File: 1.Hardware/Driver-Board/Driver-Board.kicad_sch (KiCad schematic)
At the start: 75 parts, among them J1 Conn_01x04, J2 Conn_01x02, J3 Conn_01x02, J4 Conn_01x04, J5 Conn_01x02, J6 Conn_01x02, Q1 FDN352AP, SW1 SW_Push, U1 MP2456, U2 MCP1700-3302E_SOT23, U3 TJA1051T-3, U4 AS5600, U5 TB67H450FNG,EL, U6 TB67H450FNG,EL, U7 STM32F103C6Tx, Y1 12MHz

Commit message: updated board
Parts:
- removed D1: B5819W, Diode_SMD:D_SOD-123, symbol Device:D_Schottky_Small
- L1: value L_Small -> 22uH
- SW1: footprint Button_Switch_SMD:SW_SPST_TL3305B -> custom:KMR731NG LFS
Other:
- note added: "Dual H-Bridge Drivers"
- note added: "Program using I2C"
- note removed: "Dual H-Bridge Driver"
- moved on the sheet: C11, C12, C13, C14, C15, C16, C17, C18, C2, C23, C24, C25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

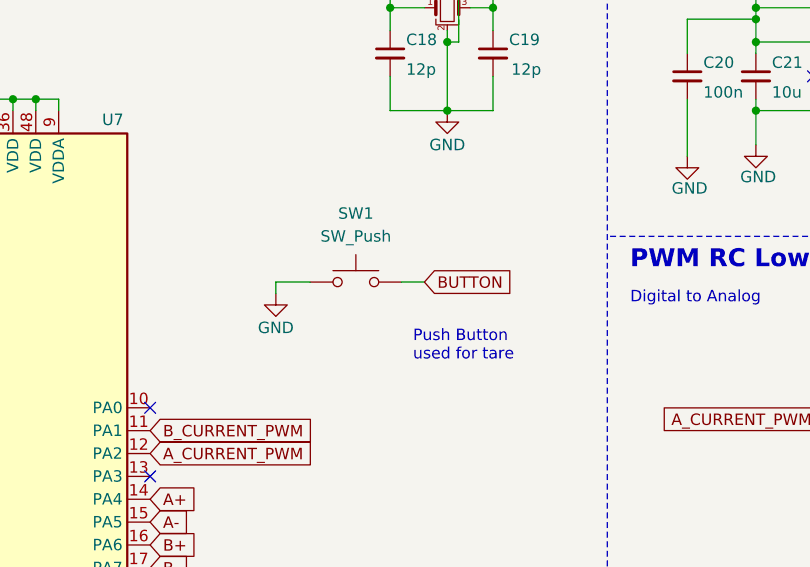
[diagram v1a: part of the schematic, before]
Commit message: libopencm3 integration and power test
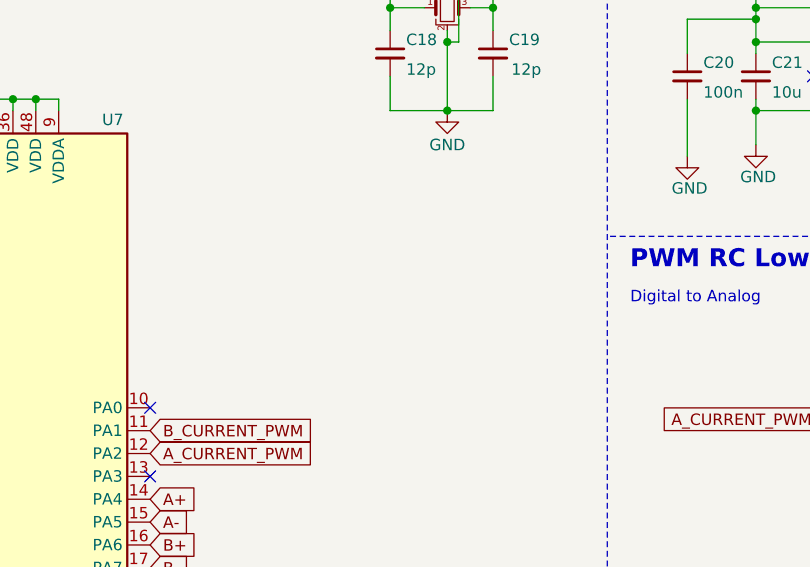
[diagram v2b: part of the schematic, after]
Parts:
- removed SW1: SW_Push, custom:KMR731NG LFS, symbol Switch:SW_Push
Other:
- note removed: "Push Button used for tare"
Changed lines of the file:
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@@
 		)
 	)
-	(wire
-		(pts
-			(xy 78.74 132.08) (xy 82.55 132.08)
-		)
-		(stroke
-			(width 0)
-			(type default)
-		)
-	)
 	(polyline
 		(pts
@@
 	(wire
 		(pts
-			(xy 78.74 133.35) (xy 78.74 132.08)
-		)
-		(stroke
-			(width 0)
-			(type default)
-		)
-	)
-	(wire
-		(pts
 			(xy 97.79 97.79) (xy 99.06 97.79)
 		)
@@
 		)
 	)
-	(wire
-		(pts
-			(xy 92.71 132.08) (xy 95.25 132.08)
-		)
-		(stroke
-			(width 0)
-			(type default)
-		)
-	)
 	(text "CAN, SWD, I2C, and Power"
 		(exclude_from_sim no)
@@
 		)
 	)
-	(text "Push Button\nused for tare"
-		(exclude_from_sim no)
-		(at 93.98 140.97 0)
-		(effects
-			(font
-				(size 1.27 1.27)
-			)
-			(justify left bottom)
-		)
-	)
 	(text "Reverse Polairty & \nOvercurrent Protection"
 		(exclude_from_sim no)
@@
 		)
 	)
-	(global_label "BUTTON"
-		(shape input)
-		(at 95.25 132.08 0)
-		(fields_autoplaced yes)
-		(effects
-			(font
-				(size 1.27 1.27)
-			)
-			(justify left)
-		)
-		(property "Intersheetrefs" "${INTERSHEET_REFS}"
-			(at 104.8598 132.1594 0)
-			(effects
-				(font
-					(size 1.27 1.27)
-				)
-				(justify left)
-				(hide yes)
-			)
-		)
-	)
 	(global_label "B_CURRENT_PWM"
 		(shape input)
@@
 	)
 	(symbol
-		(lib_id "Switch:SW_Push")
-		(at 87.63 132.08 0)
-		(unit 1)
-		(exclude_from_sim no)
-		(in_bom yes)
-		(on_board yes)
-		(dnp no)
-		(fields_autoplaced yes)
-		(property "Reference" "SW1"
-			(at 87.63 124.46 0)
-			(effects
-				(font
-					(size 1.27 1.27)
-				)
-			)
-		)
-		(property "Value" "SW_Push"
-			(at 87.63 127 0)
-			(effects
-				(font
-					(size 1.27 1.27)
-				)
-			)
-		)
-		(property "Footprint" "custom:KMR731NG LFS"
-			(at 87.63 127 0)
-			(effects
-				(font
-					(size 1.27 1.27)
-				)
-				(hide yes)
-			)
-		)
-		(property "Datasheet" "~"
-			(at 87.63 127 0)
-			(effects
-				(font
-					(size 1.27 1.27)
-				)
-				(hide yes)
-			)
-		)
-		(property "Description" ""
-			(at 87.63 132.08 0)
-			(effects
-				(font
-					(size 1.27 1.27)
-				)
-				(hide yes)
-			)
-		)
-		(pin "1"
-		)
-		(pin "2"
-		)
-		(instances
-			(project ""
-				(path "/d43c9ddf-895f-499e-825c-a7474ad7dc92"
-					(reference "SW1")
-					(unit 1)
-				)
-			)
-		)
-	)
-	(symbol
 		(lib_id "Device:Crystal_GND24_Small")
 		(at 97.79 101.6 0)
@@
 					(unit 1)
 				)
-			)
-		)
-	)
-	(symbol
-		(lib_id "power:GND")
-		(at 78.74 133.35 0)
-		(unit 1)
-		(exclude_from_sim no)
-		(in_bom yes)
-		(on_board yes)
-		(dnp no)
-		(property "Reference" "#PWR045"
-			(at 78.74 139.7 0)
-			(effects
-				(font
-					(size 1.27 1.27)
-				)
-				(hide yes)
-			)
-		)
-		(property "Value" "GND"
-			(at 78.74 137.16 0)
-			(effects
-				(font
-					(size 1.27 1.27)
-				)
-			)
-		)
-		(property "Footprint" ""
-			(at 78.74 133.35 0)
-			(effects
-				(font
-					(size 1.27 1.27)
-				)
-				(hide yes)
-			)
-		)
-		(property "Datasheet" ""
-			(at 78.74 133.35 0)
-			(effects
-				(font
-					(size 1.27 1.27)
-				)
-				(hide yes)
-			)
-		)
-		(property "Description" ""
-			(at 78.74 133.35 0)
-			(effects
-				(font
-					(size 1.27 1.27)
-				)
-				(hide yes)
-			)
-		)
-		(pin "1"
-		)
-		(instances
-			(project ""
-				(path "/d43c9ddf-895f-499e-825c-a7474ad7dc92"
-					(reference "#PWR045")
-					(unit 1)
-				)
